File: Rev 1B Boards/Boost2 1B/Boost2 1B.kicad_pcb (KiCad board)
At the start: 2 copper layers, 39 parts, among them J27 Banana 2P, J28 Banana 2P, Q1 BSC059N04LS6, Q2 BSC059N04LS6, U1 TPS43061

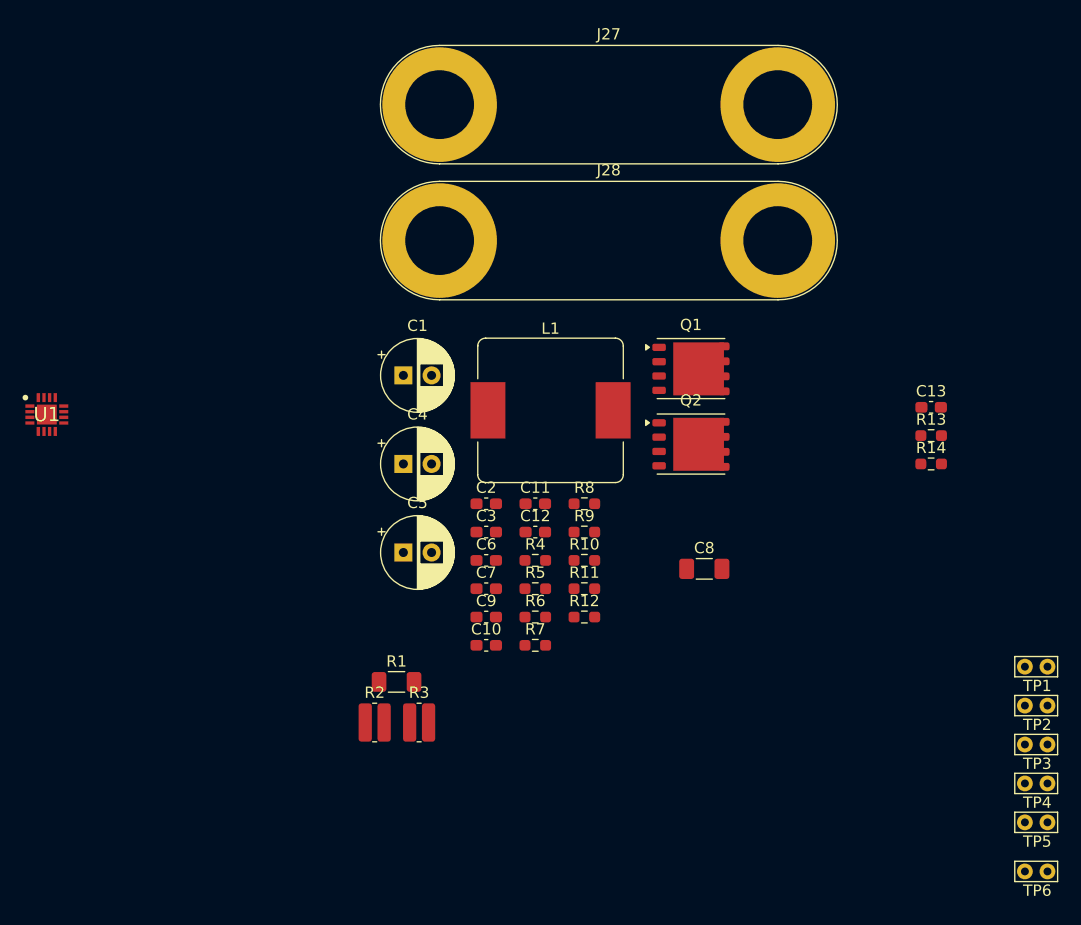
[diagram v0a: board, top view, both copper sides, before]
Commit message: Complete boost2 layout
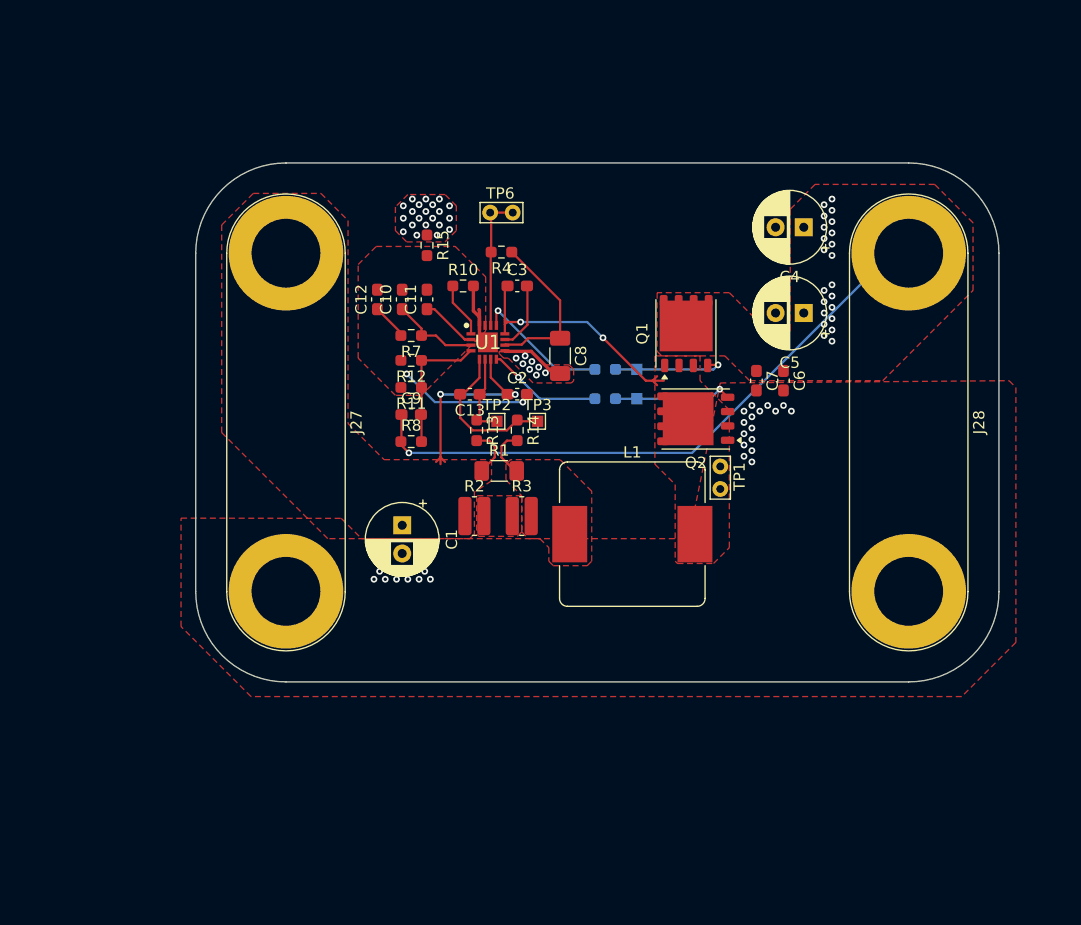
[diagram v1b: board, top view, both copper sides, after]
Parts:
- removed R5: 0, Resistor_SMD:R_0603_1608Metric_Pad0.98x0.95mm_HandSolder
- added R15: 0, Resistor_SMD:R_0603_1608Metric_Pad0.98x0.95mm_HandSolder, F.Cu at (118.4, 80.8)
- R6, R9: moved to B.Cu
- TP2, TP3: footprint TestPoint:TestPoint_Bridge_Pitch2.0mm_Drill0.7mm -> TestPoint:TestPoint_Pad_1.0x1.0mm
- TP4, TP5: footprint TestPoint:TestPoint_Bridge_Pitch2.0mm_Drill0.7mm -> TestPoint:TestPoint_Pad_1.0x1.0mm; moved to B.Cu
- moved TP6 74.0 mm to (126.0, 77.9), turned to 180 degrees
- moved TP2 53.2 mm to (124.6, 96.4)
- moved TP5 52.9 mm to (137.0, 91.8)
- moved TP3 51.8 mm to (128.2, 96.4)
- moved TP4 48.4 mm to (137.0, 94.4)
- moved J28 41.6 mm to (161.1, 81.5), turned to -90 degrees
- moved C5 41.4 mm to (151.8, 86.8), turned to 180 degrees
- moved C4 41.2 mm to (151.8, 79.2), turned to 180 degrees
- moved C13 40.9 mm to (122.2, 94.0), turned to 180 degrees
- moved R13 40.3 mm to (122.8, 97.2), turned to -90 degrees
- moved U1 39.6 mm to (123.8, 89.4)
- moved R14 36.8 mm to (126.4, 97.2), turned to -90 degrees
- moved C10 31.6 mm to (116.2, 85.6), turned to 90 degrees
- moved TP1 31.3 mm to (144.4, 102.4), turned to 90 degrees
- moved C6 30.8 mm to (150.0, 92.8), turned to -90 degrees
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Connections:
- C10 pad 2: GNDPWR -> /Output Boost (Stage 2)/AGND
- C11 pad 2: GNDPWR -> /Output Boost (Stage 2)/AGND
- C12 pad 2: GNDPWR -> /Output Boost (Stage 2)/AGND
- C2 pad 2: GNDPWR -> /Output Boost (Stage 2)/AGND
- C8 pad 2: /Output Boost (Stage 2)/PGND -> GNDPWR
- Q2 pad 1: /Output Boost (Stage 2)/PGND -> GNDPWR
- Q2 pad 2: /Output Boost (Stage 2)/PGND -> GNDPWR
- Q2 pad 3: /Output Boost (Stage 2)/PGND -> GNDPWR
- R10 pad 2: GNDPWR -> /Output Boost (Stage 2)/AGND
- R11 pad 2: GNDPWR -> /Output Boost (Stage 2)/AGND
- R12 pad 2: GNDPWR -> /Output Boost (Stage 2)/AGND
- U1 pad 16: GNDPWR -> /Output Boost (Stage 2)/AGND
- U1 pad 17: GNDPWR -> /Output Boost (Stage 2)/AGND
- U1 pad 7: /Output Boost (Stage 2)/ISNS+ -> /+4.4V_{SCAP}_IN
- U1 pad 9: /Output Boost (Stage 2)/PGND -> GNDPWR
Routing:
- net /+24V_CAP_OUT: track 0.00 -> 55.3 mm, vias 0 -> 1
- net /+4.4V_{SCAP}_IN: track 0.00 -> 22.9 mm, vias 0 -> 2
- net /Output Boost (Stage 2)/SW: track 0.00 -> 22.4 mm, vias 0 -> 2
- net /Output Boost (Stage 2)/AGND: track 0.00 -> 19.1 mm, vias 0 -> 2
- net /Output Boost (Stage 2)/VCC: track 0.00 -> 14.6 mm
- net /Output Boost (Stage 2)/ISNS-: track 0.00 -> 13.8 mm
- net /Output Boost (Stage 2)/HDRV: track 0.00 -> 12.1 mm, vias 0 -> 1
- net /Output Boost (Stage 2)/PGOOD: track 0.00 -> 12.1 mm
- net /Output Boost (Stage 2)/FB: track 0.00 -> 12.0 mm
- net /Output Boost (Stage 2)/LDRV_R: track 0.00 -> 10.6 mm, vias 0 -> 1
- net /Output Boost (Stage 2)/HDRV_R: track 0.00 -> 10.2 mm, vias 0 -> 1
- net /Output Boost (Stage 2)/LDRV: track 0.00 -> 10.2 mm, vias 0 -> 1
- net /Output Boost (Stage 2)/COMP: track 0.00 -> 7.79 mm
- net /Output Boost (Stage 2)/ISNS+: track 0.00 -> 7.54 mm
- net /Output Boost (Stage 2)/BOOT: track 0.00 -> 6.00 mm
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- added copper zone on F.Cu, net /+24V_CAP_OUT
- added copper zone on F.Cu, net /+4.4V_{SCAP}_IN
- added copper zone on F.Cu, net /Output Boost (Stage 2)/AGND
- added copper zone on F.Cu, net /Output Boost (Stage 2)/IN_R
- added copper zone on F.Cu, net /Output Boost (Stage 2)/IN_RR
- added copper zone on F.Cu, net /Output Boost (Stage 2)/SW
- added copper zone on F.Cu, net GNDPWR
- added copper zone on In1.Cu, net GNDPWR
- added copper zone on In2.Cu, net GNDPWR
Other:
- board outline added: 71.2 x 46 mm
- copper layers 2 -> 4

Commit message: Fix DRC issues
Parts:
- moved TP2 0.10 mm to (124.6, 96.5)
- moved TP3 0.10 mm to (128.2, 96.5)
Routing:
- net /+24V_CAP_OUT: track 55.3 -> 61.1 mm
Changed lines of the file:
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@@
 			(at 14.985 -6.24 90)
 			(layer "F.SilkS")
+			(hide yes)
 			(effects
 				(font
@@
 		(tags "resistor handsolder")
 		(property "Reference" "R8"
-			(at 0 -1.43 0)
+			(at -2.9 0 0)
 			(layer "F.SilkS")
 			(effects
@@
 		(tags "capacitor handsolder")
 		(property "Reference" "C10"
-			(at 0 -1.43 90)
+			(at 3.3 0 90)
 			(layer "F.SilkS")
 			(effects
@@
 		(tags "resistor handsolder")
 		(property "Reference" "R3"
-			(at 0 -2.65 0)
+			(at 0 2.8 0)
 			(layer "F.SilkS")
 			(effects
@@
 		(tags "resistor handsolder")
 		(property "Reference" "R2"
-			(at 0 -2.65 0)
+			(at 0 2.8 0)
 			(layer "F.SilkS")
 			(effects
@@
 		(tags "capacitor handsolder")
 		(property "Reference" "C12"
-			(at 0 -1.43 90)
+			(at 3.3 0.1 90)
 			(layer "F.SilkS")
 			(effects
@@
 		(tags "resistor handsolder")
 		(property "Reference" "R14"
-			(at 0 -1.43 90)
+			(at 1.7 -1.6 90)
 			(layer "F.SilkS")
 			(effects
@@
 		(tags "resistor handsolder")
 		(property "Reference" "R12"
-			(at 0 -1.43 0)
+			(at 3.4 0 0)
 			(layer "F.SilkS")
 			(effects
@@
 	(footprint "TestPoint:TestPoint_Pad_1.0x1.0mm"
 		(layer "F.Cu")
-		(at 128.2 96.4)
+		(at 128.2 96.5)
 		(descr "SMD rectangular pad as test Point, square 1.0mm side length")
 		(tags "test point SMD pad rectangle square")
@@
 			(at 0 -1.448 0)
 			(layer "F.SilkS")
+			(hide yes)
 			(effects
 				(font
@@
 			(at 14.985 -6.24 90)
 			(layer "F.SilkS")
+			(hide yes)
 			(effects
 				(font
@@
 		(tags "Integrated Circuit")
 		(property "Reference" "U1"
-			(at 0 0 0)
+			(at -3.3 0 90)
 			(layer "F.SilkS")
 			(effects
@@
 		(tags "capacitor handsolder")
 		(property "Reference" "C7"
-			(at 0 -1.43 90)
+			(at -0.6 1.5 90)
 			(layer "F.SilkS")
 			(effects
@@
 		(tags "CP Radial series Radial pin pitch 2.50mm  diameter 6.3mm Electrolytic Capacitor")
 		(property "Reference" "C4"
-			(at 1.25 -4.4 0)
+			(at 5.5 0 90)
 			(layer "F.SilkS")
 			(effects
@@
 		(tags "Infineon OptiMOS")
 		(property "Reference" "Q2"
-			(at 0 -3.9 0)
+			(at 4.625 -0.025 90)
 			(layer "F.SilkS")
 			(effects
@@
 		(tags "capacitor handsolder")
 		(property "Reference" "C11"
-			(at 0 -1.43 90)
+			(at -0.9 1.6 90)
 			(layer "F.SilkS")
 			(effects
@@
 			(at 1.1 1.7 90)
 			(layer "F.SilkS")
+			(hide yes)
 			(effects
 				(font
@@
 		(tags "CP Radial series Radial pin pitch 2.50mm  diameter 6.3mm Electrolytic Capacitor")
 		(property "Reference" "C1"
-			(at 1.25 -4.4 90)
+			(at -2.917621 0 180)
 			(layer "F.SilkS")
 			(effects
@@
 		(tags "resistor handsolder")
 		(property "Reference" "R4"
-			(at 0 -1.43 0)
+			(at -2.7 0 0)
 			(layer "F.SilkS")
 			(effects
@@
 		(tags "capacitor handsolder")
 		(property "Reference" "C13"
-			(at 0 -1.43 0)
+			(at 0 1.4 0)
 			(layer "F.SilkS")
 			(effects
@@
 		(tags "resistor handsolder")
 		(property "Reference" "R13"
-			(at 0 -1.43 90)
+			(at 0 1.5 90)
 			(layer "F.SilkS")
 			(effects
@@
 	(footprint "TestPoint:TestPoint_Pad_1.0x1.0mm"
 		(layer "F.Cu")
-		(at 124.6 96.4)
+		(at 124.6 96.5)
 		(descr "SMD rectangular pad as test Point, square 1.0mm side length")
 		(tags "test point SMD pad rectangle square")
@@
 			(at 0 -1.448 0)
 			(layer "F.SilkS")
+			(hide yes)
 			(effects
 				(font
@@
 			(at 1.1 1.7 0)
 			(layer "F.SilkS")
+			(hide yes)
 			(effects
 				(font
@@
 		(tags "capacitor handsolder")
 		(property "Reference" "C9"
-			(at 0 -1.43 0)
+			(at -2.9 0 0)
 			(layer "F.SilkS")
 			(effects
@@
 		(tags "resistor handsolder")
 		(property "Reference" "R7"
-			(at 0 -1.43 0)
+			(at 3 0 0)
 			(layer "F.SilkS")
 			(effects
@@
 		(tags "CP Radial series Radial pin pitch 2.50mm  diameter 6.3mm Electrolytic Capacitor")
 		(property "Reference" "C5"
-			(at 1.25 -4.4 0)
+			(at 5.5 -0.1 90)
 			(layer "F.SilkS")
 			(effects
@@
 		(tags "resistor handsolder")
 		(property "Reference" "R11"
-			(at 0 -1.43 0)
+			(at 3.3 0 0)
 			(layer "F.SilkS")
 			(effects
@@
 			(at 0 1.448 180)
 			(layer "B.SilkS")
+			(hide yes)
 			(effects
 				(font
@@
 		(tags "resistor handsolder")
 		(property "Reference" "R9"
-			(at 0 1.43 180)
+			(at 0 -1.4 180)
 			(layer "B.SilkS")
 			(effects
@@
 			(at 0 1.448 180)
 			(layer "B.SilkS")
+			(hide yes)
 			(effects
 				(font
@@
 	)
 	(segment
-		(start 116.8 99.2)
-		(end 141.9 99.2)
+		(start 161.1 88.684204)
+		(end 157.684204 92.1)
+		(width 0.2)
+		(layer "B.Cu")
+		(net 5)
+	)
+	(segment
+		(start 157.684204 92.1)
+		(end 148.2 92.1)
 		(width 0.2)
 		(layer "B.Cu")
@@
 	)
 	(segment
-		(start 141.9 99.2)
-		(end 159.6 81.5)
+		(start 161.1 81.5)
+		(end 161.1 88.684204)
+		(width 0.2)
+		(layer "B.Cu")
+		(net 5)
+	)
+	(segment
+		(start 141.1 99.2)
+		(end 116.8 99.2)
 		(width 0.2)
 		(layer "B.Cu")
@@
 	)
 	(segment
+		(start 148.2 92.1)
+		(end 141.1 99.2)
+		(width 0.2)
+		(layer "B.Cu")
+		(net 5)
+	)
+	(segment
 		(start 130.2 85.6875)
 		(end 125.9125 81.4)
@@
 	)
 	(segment
-		(start 122.457866 97.201)
-		(end 121.3375 96.080634)
+		(start 128.1 96.4)
+		(end 126.5125 96.4)
 		(width 0.2)
 		(layer "F.Cu")
@@
 	)
 	(segment
-		(start 128.2 96.4)
-		(end 126.5125 96.4)
+		(start 128.2 96.5)
+		(end 128.1 96.4)
 		(width 0.2)
 		(layer "F.Cu")
@@
 	)
 	(segment
-		(start 126.5125 96.4)
-		(end 126.4 96.2875)
+		(start 122.556866 97.3)
+		(end 121.3375 96.080634)
 		(width 0.2)
 		(layer "F.Cu")
@@
 	)
 	(segment
-		(start 126.4 96.2875)
-		(end 125.4865 97.201)
+		(start 126.5125 96.4)
+		(end 126.4 96.2875)
 		(width 0.2)
 		(layer "F.Cu")
@@
 	)
 	(segment
-		(start 125.4865 97.201)
-		(end 122.457866 97.201)
+		(start 121.3375 96.080634)
+		(end 121.3375 94)
 		(width 0.2)
 		(layer "F.Cu")
@@
 	)
 	(segment
+		(start 126.4 96.2875)
+		(end 125.3875 97.3)
+		(width 0.2)
+		(layer "F.Cu")
+		(net 11)
+	)
+	(segment
 		(start 121.6 94)
 		(end 121.3375 94)
@@
 	)
 	(segment
-		(start 121.3375 96.080634)
-		(end 121.3375 94)
+		(start 125.3875 97.3)
+		(end 122.556866 97.3)
 		(width 0.2)
 		(layer "F.Cu")
@@
 	)
 	(segment
+		(start 124.6 96.5)
+		(end 124.5 96.4)
+		(width 0.2)
+		(layer "F.Cu")
+		(net 20)
+	)
+	(segment
 		(start 123.55 93.5125)
 		(end 123.0625 94)
@@
 	)
 	(segment
-		(start 123.0625 96.025)
+		(start 122.9125 96.4)
 		(end 122.8 96.2875)
 		(width 0.2)
@@
 	)
 	(segment
-		(start 124.6 96.4)
+		(start 124.5 96.4)
 		(end 122.9125 96.4)
 		(width 0.2)
@@
 	)
 	(segment
-		(start 123.0625 94)
-		(end 123.0625 96.025)
+		(start 123.0625 96.025)
+		(end 122.8 96.2875)
 		(width 0.2)
 		(layer "F.Cu")
@@
 	)
 	(segment
-		(start 122.9125 96.4)
-		(end 122.8 96.2875)
+		(start 123.0625 94)
+		(end 123.0625 96.025)
 		(width 0.2)
 		(layer "F.Cu")

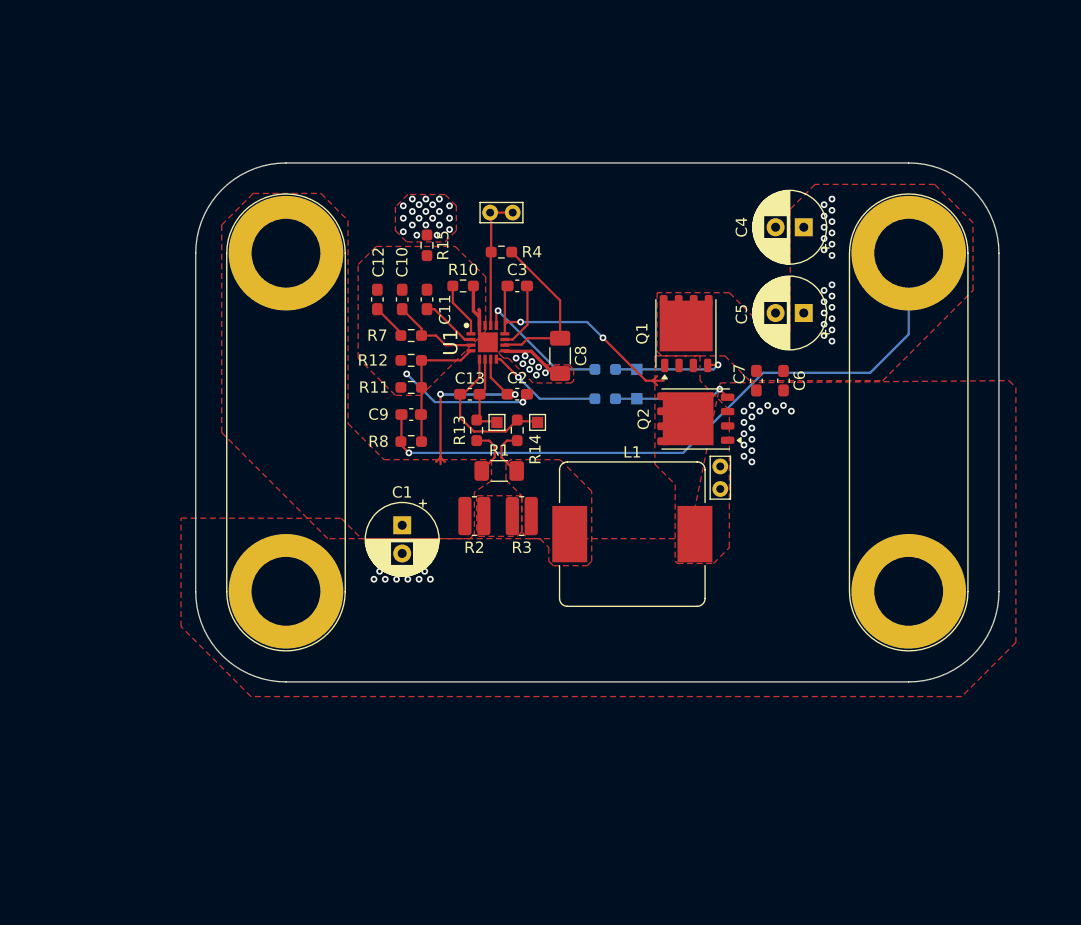
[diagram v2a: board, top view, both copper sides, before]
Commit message: Label boost2 board
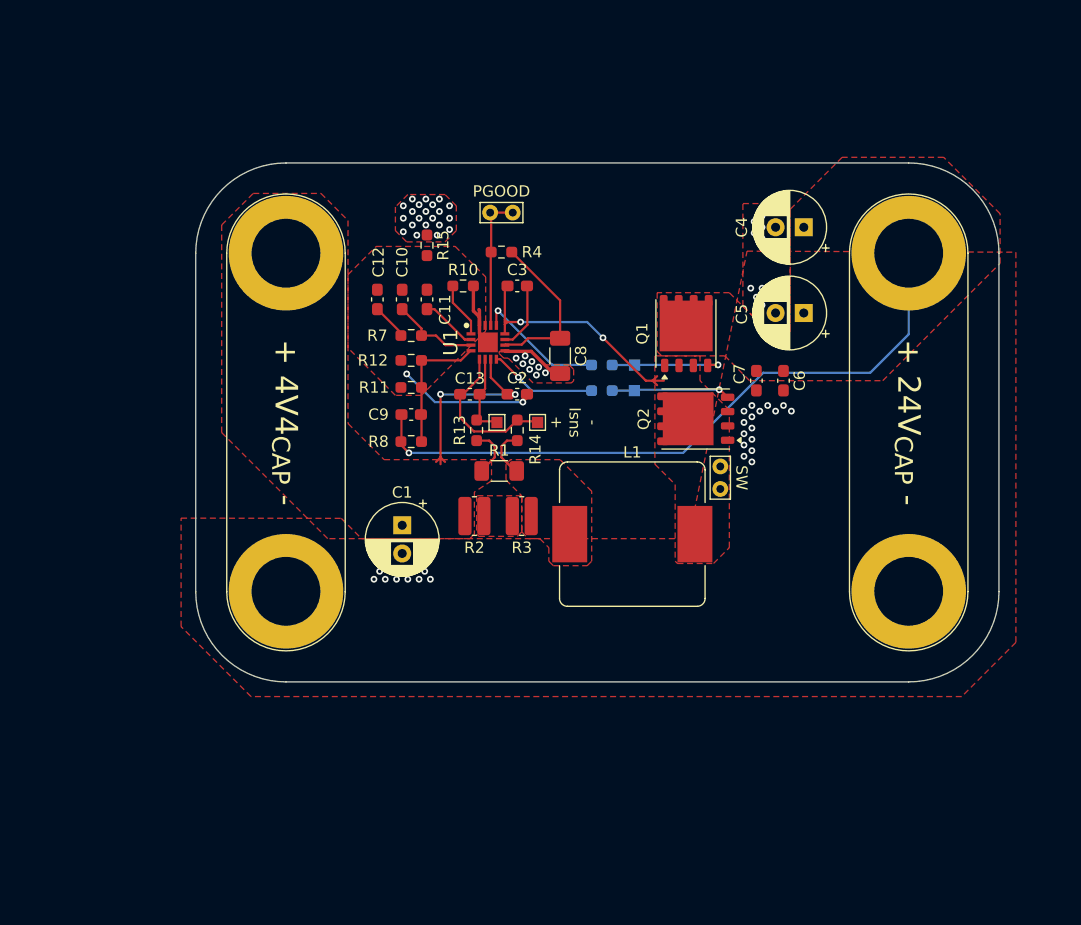
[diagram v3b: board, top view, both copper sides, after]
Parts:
- added G***: LOGO, ! Robomaster Special:StampedeLogo, B.Cu at (133.5, 81.5)
- moved R6 0.78 mm to (133.9, 93.7)
- moved TP4 0.75 mm to (136.8, 93.7)
- moved R9 0.49 mm to (133.9, 91.4)
- moved TP5 0.44 mm to (136.8, 91.4)
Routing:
- net /Output Boost (Stage 2)/LDRV: track 10.2 -> 9.60 mm
- net GNDPWR: vias 78 -> 70
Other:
- board text added: "+ 24V_{CAP} -"
- board text added: "+ 4V4_{CAP} -"
- board text added: "- Isns +"
- board text added: "HDRV"
- board text added: "LDRV"
- board text added: "PGOOD"
- board text added: "SW"
- board text added: "UT Stampede Supercapacitor Second Boost _{Jed Wang}"
